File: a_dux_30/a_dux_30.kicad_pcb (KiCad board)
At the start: 2 copper layers, 129.4 x 98.7 mm, 32 parts

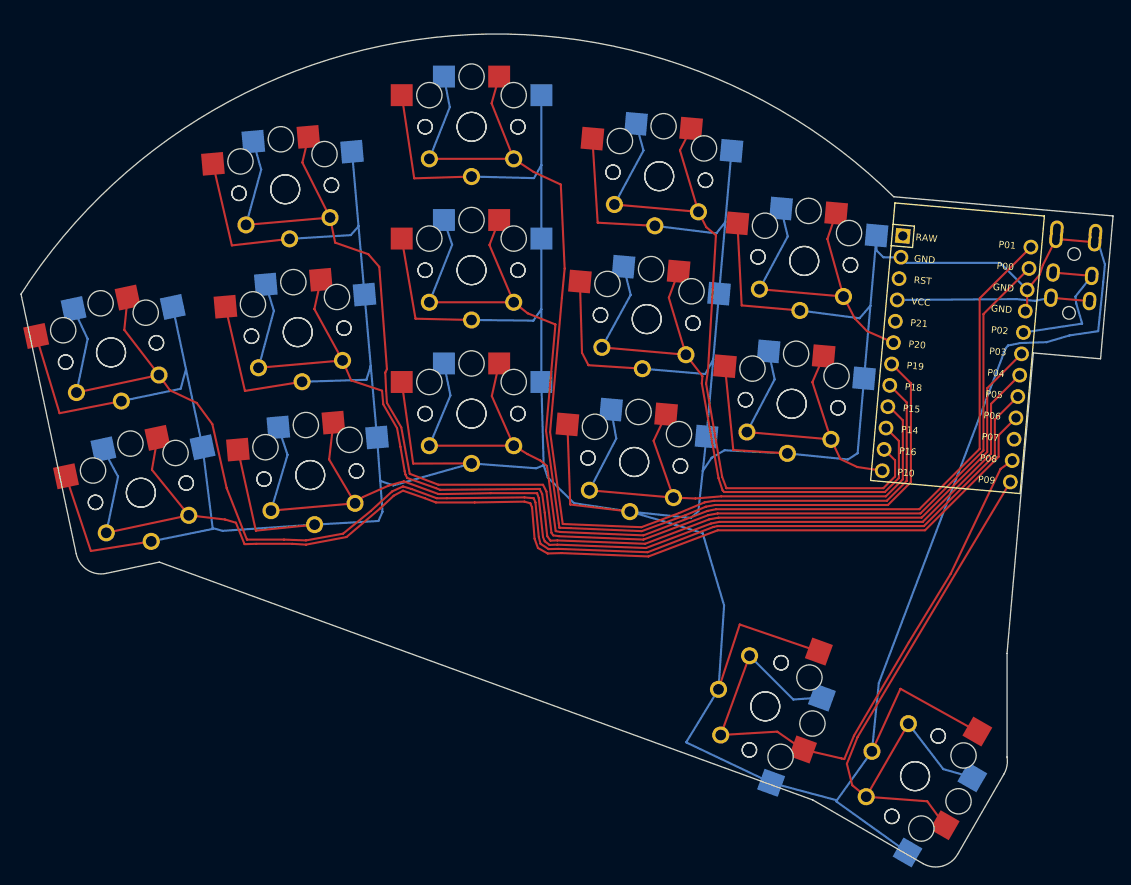
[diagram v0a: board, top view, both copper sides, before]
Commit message: fillet tracks
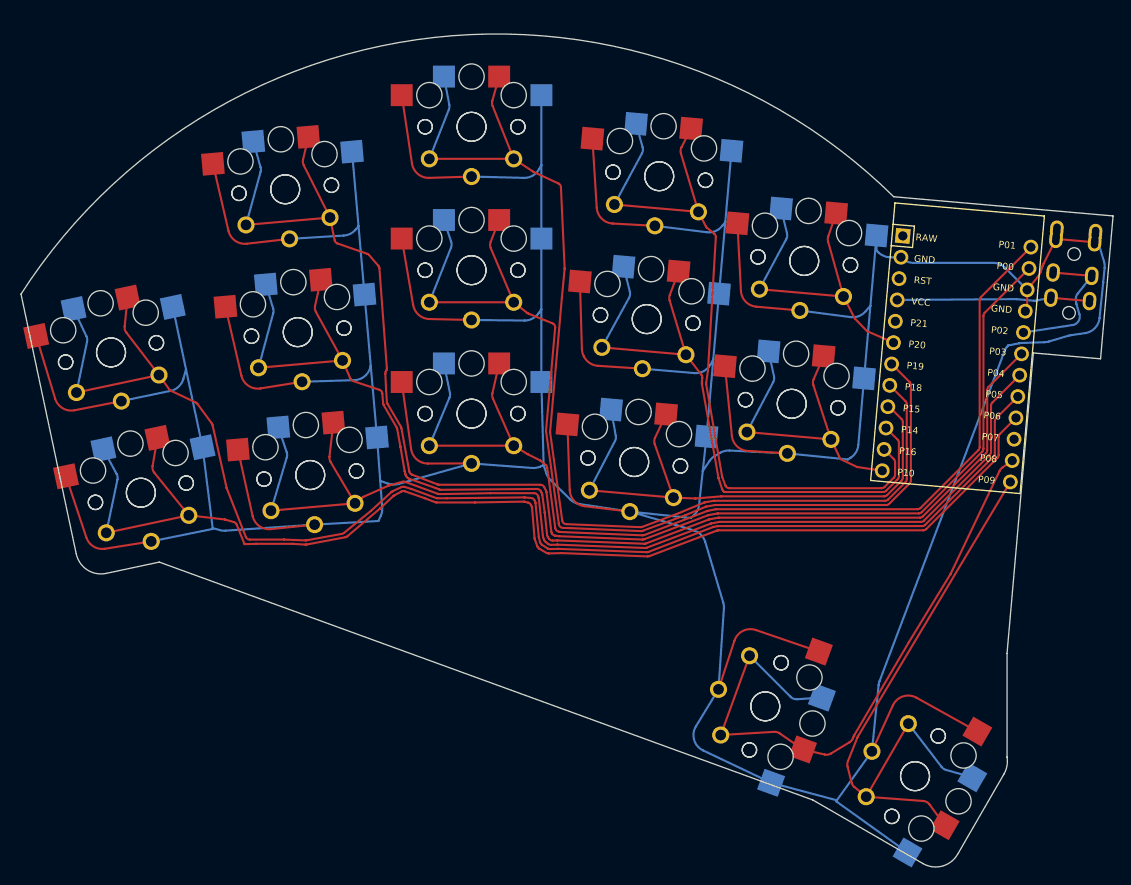
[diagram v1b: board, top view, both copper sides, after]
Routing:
- net GND: track 779.9 -> 764.7 mm
- net P8: track 77.0 -> 75.8 mm
- net P2: track 18.1 -> 17.4 mm

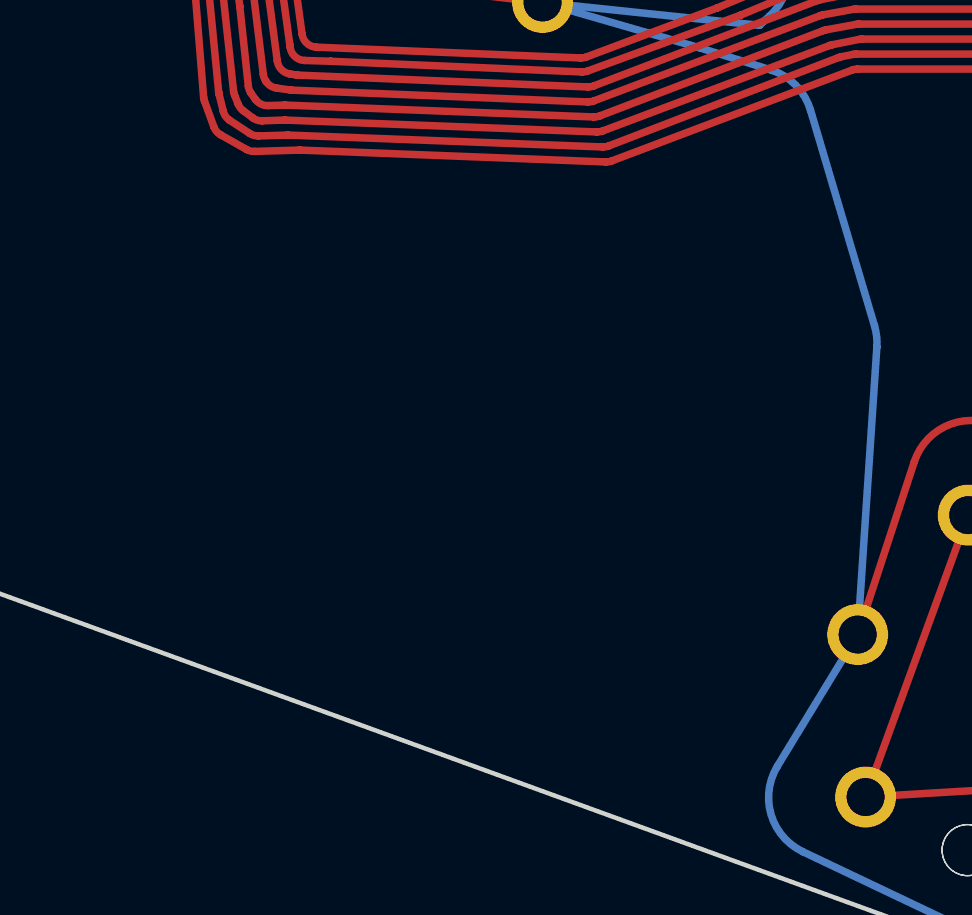
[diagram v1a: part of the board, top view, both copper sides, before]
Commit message: add silkscreen
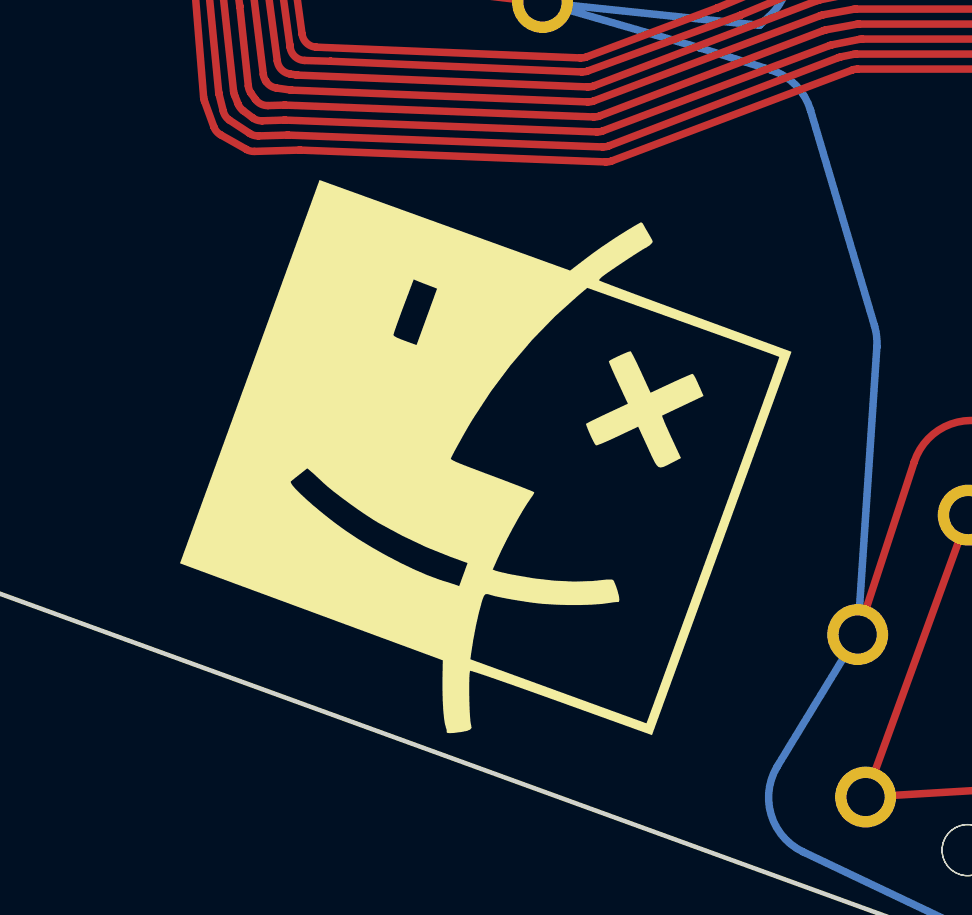
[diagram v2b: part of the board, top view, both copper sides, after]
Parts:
- added ?: LOGO, logo:logo, F.Cu at (67.1, 1.07)
- added ?: LOGO, logo:logo, B.Cu at (67.1, 1.04)

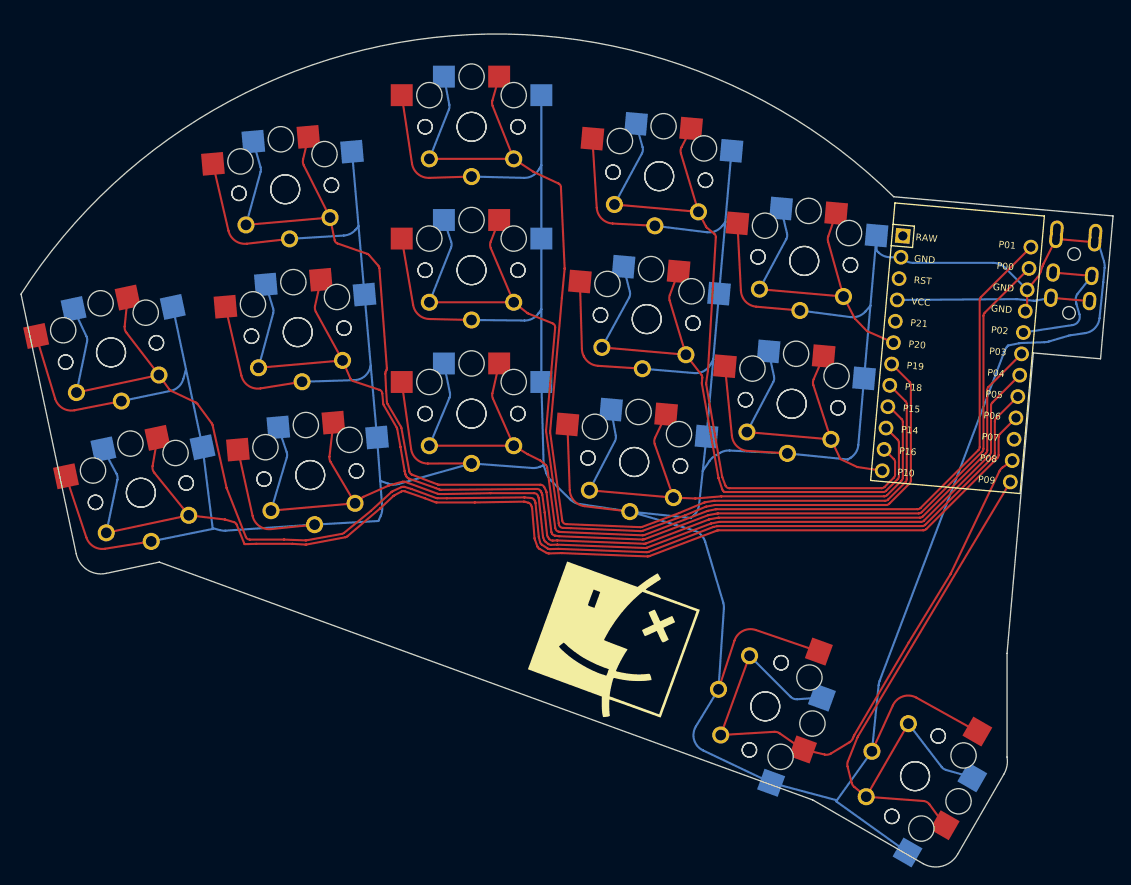
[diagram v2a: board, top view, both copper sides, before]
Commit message: add teardrops
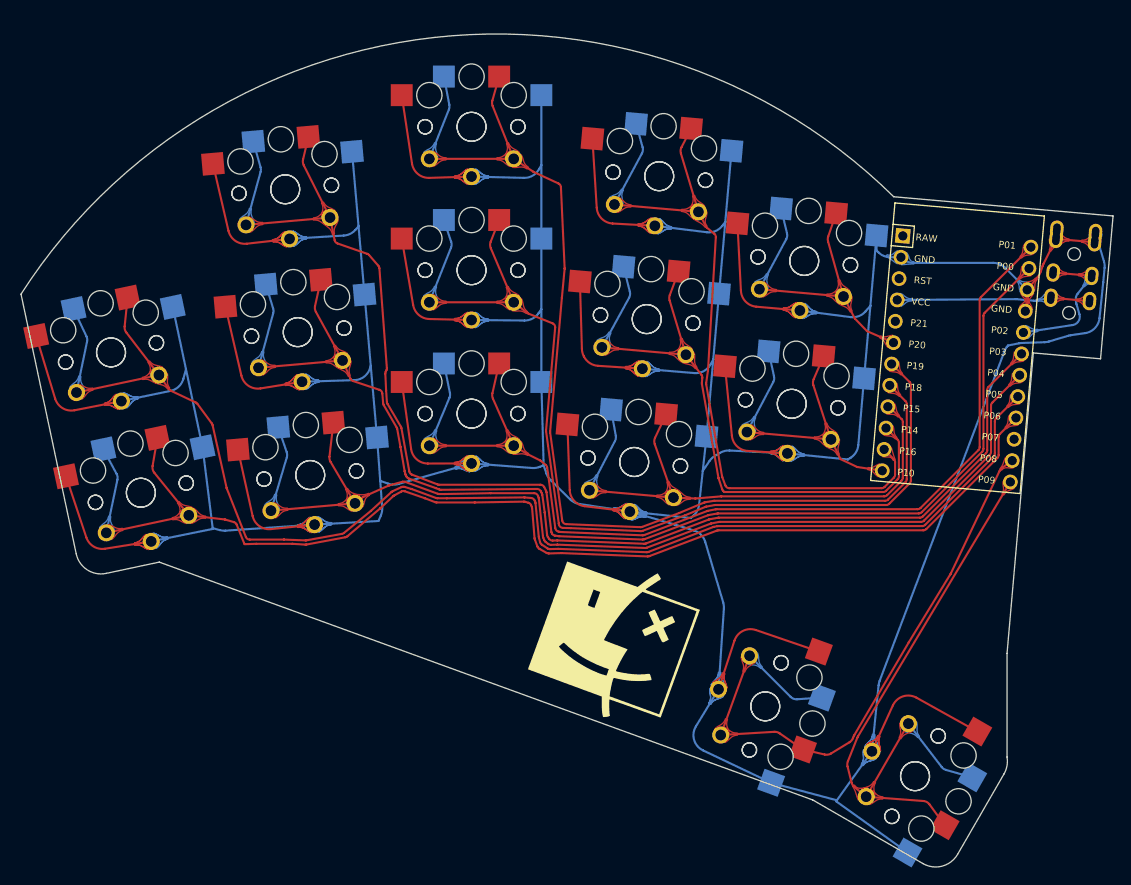
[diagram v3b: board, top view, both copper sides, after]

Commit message: A dux 30 rev2 (#2)
* increase pinky stagger

* reduce middle-index gap

* move thumbs in towards palm

* add version metadata

* remove unused binds

* ignore node

* add alias for ergogen cli

* add author meta

* update pcb

* redo pin layout

* remove corners

* remove thumb extension outline

* add extra bind to cover hotswap pads around thumbs

* redo pin layout for ring column

* move trrs jack below mcu

* compact pin layouts

* add routes

* add art

* add rendered images of rev2

* add teardrops

* add sketchy rounding/fillet

* new gerbers

* new gerbers

* fix incorrect pin for trrs

* add Makefile
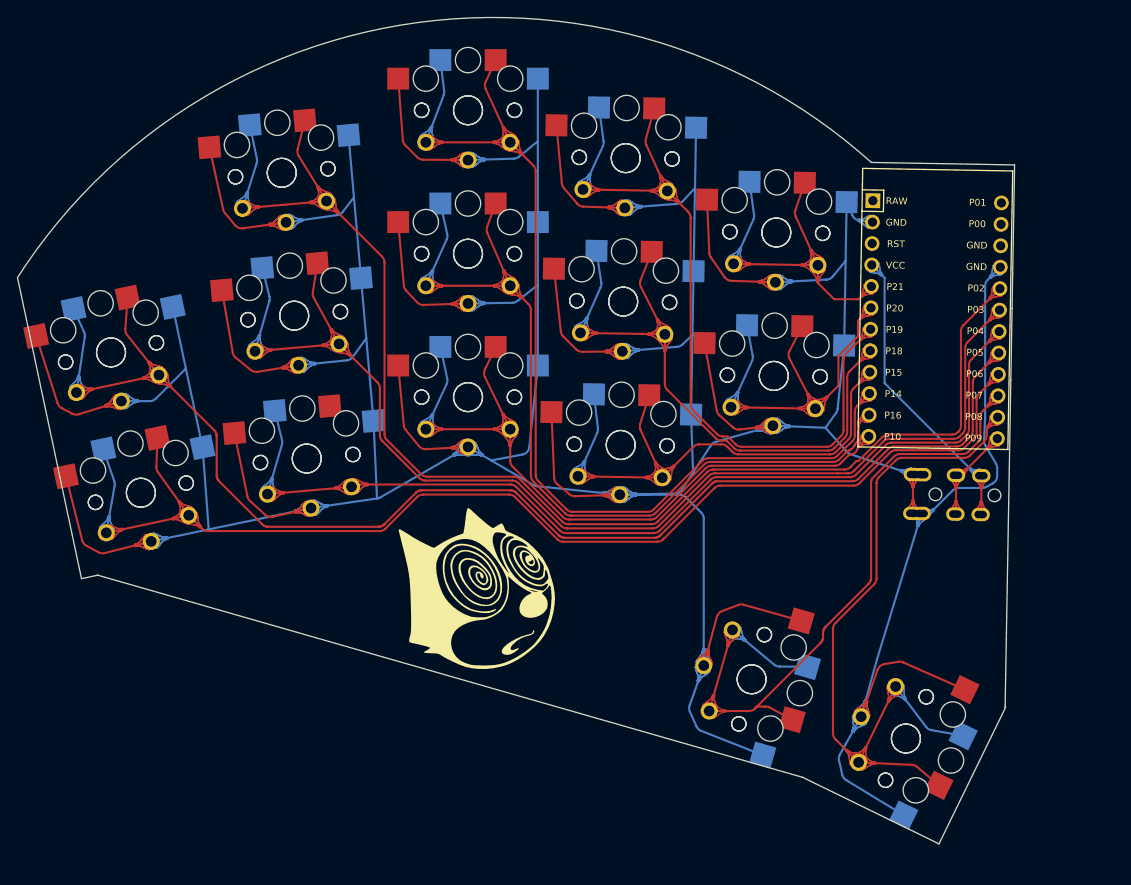
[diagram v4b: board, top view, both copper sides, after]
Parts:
- removed ? (x2): LOGO, logo:logo
- added G***: LOGO, logos:felix_dazed, F.Cu at (52.8, -4.65)
- added G***: LOGO, logos:felix_love, B.Cu at (52.2, -5.35)
- moved REF** 23.1 mm to (113.7, -13.6), turned to -91 degrees
- moved MCU1 5.30 mm to (105.1, -36.8), turned to -91 degrees
- moved S25 4.72 mm to (86.2, -47.1), turned to -1 degrees
- moved S26 4.72 mm to (86.2, -47.1), turned to 179 degrees
- moved S29 4.60 mm to (101.6, 12.9), turned to -116 degrees
- moved S30 4.60 mm to (101.6, 12.9), turned to 64 degrees
- moved S21 4.51 mm to (68.4, -55.9), turned to -1 degrees
- moved S22 4.51 mm to (68.4, -55.9), turned to 179 degrees
- moved S23 3.93 mm to (86.0, -30.1), turned to -1 degrees
- moved S24 3.93 mm to (86.0, -30.1), turned to 179 degrees
- moved S27 3.59 mm to (83.3, 5.86), turned to -106 degrees
- moved S28 3.59 mm to (83.3, 5.86), turned to 74 degrees
- moved S19 3.48 mm to (68.1, -38.9), turned to -1 degrees
- moved S20 3.48 mm to (68.1, -38.9), turned to 179 degrees
- moved S17 2.58 mm to (67.8, -21.9), turned to -1 degrees
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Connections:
- REF** pad 3: P2 -> P9
- S10 pad 1: P0 -> P2
- S11 pad 1: P1 -> P10
- S12 pad 1: P1 -> P10
- S13 pad 1: P19 -> P16
- S14 pad 1: P19 -> P16
- S15 pad 1: P18 -> P14
- S16 pad 1: P18 -> P14
- S19 pad 1: P14 -> P18
- S20 pad 1: P14 -> P18
- S21 pad 1: P16 -> P19
- S22 pad 1: P16 -> P19
- S23 pad 1: P10 -> P20
- S24 pad 1: P10 -> P20
- S25 pad 1: P20 -> P21
- S26 pad 1: P20 -> P21
- S27 pad 1: P8 -> P7
- S28 pad 1: P8 -> P7
- S29 pad 1: P9 -> P8
- S30 pad 1: P9 -> P8
- S9 pad 1: P0 -> P2
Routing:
- net P0: track 165.3 -> 0.00 mm
- net P2: track 17.4 -> 157.0 mm
- net P1: track 123.1 -> 0.00 mm
- net P7: track 0.00 -> 84.3 mm
- net P9: track 74.4 -> 11.3 mm
- net P18: track 131.6 -> 73.6 mm
- net P10: track 38.7 -> 84.4 mm
- net P14: track 76.0 -> 120.7 mm
- net P21: track 0.00 -> 40.7 mm
- net GND: track 764.7 -> 735.6 mm
- net P19: track 118.7 -> 91.5 mm
- net P16: track 88.9 -> 102.5 mm
- net P4: track 126.4 -> 113.9 mm
- net VCC: track 22.9 -> 35.3 mm
- net P8: track 75.8 -> 85.6 mm
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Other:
- board size 129.4 x 98.7 mm -> 118.2 x 97.9 mm
